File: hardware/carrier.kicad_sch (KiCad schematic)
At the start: 58 parts, among them J2 Heltec_J2, J3 Heltec_J3, U1 MT3608, U2 TCA9534PWR, U3 MAX98357A

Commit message: hardware: regenerate for 4-pin XH, add XB8089D cell protection, power model
Regenerated with KiCad 9 after the cloud parts review (make all: ERC 0, DRC 0,
0 unrouted). Six 4-pin XH connectors do not fit the top edge, so J_BTN_R1 moves
to the bottom edge under J2; the schematic connectors shift because Conn_01x04
anchors on pin 2. Two-wire connectors label only pins 1-2 on silk.

The Heltec V4.2 schematic shows no under-voltage cutoff (CN3165 charger, Q4 is
reverse-polarity only), so U4 XB8089D (C79928) goes in the cell negative lead
with R_PROT1 1k / C_PROT1 100nF. Symbol lives in the project lib local.kicad_sym.

power_budget.py estimates runtime per scenario from the Heltec datasheet and
marked estimates (~25 h Deluxe game with backlight, ~40 h without).

Co-Authored-By: Claude Opus 5.5 <noreply@anthropic.com>
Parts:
- added C_PROT1: 100nF, Capacitor_SMD:C_0805_2012Metric_Pad1.18x1.45mm_HandSolder, symbol Device:C
- added R_PROT1: 1k, Resistor_SMD:R_0805_2012Metric_Pad1.20x1.40mm_HandSolder, symbol Device:R
- added U4: XB8089D, Package_SO:SOIC-8-1EP_3.9x4.9mm_P1.27mm_EP2.41x3.3mm, symbol local:XB8089D
- J_BAT1, J_BUZ1, J_HBAT1, J_KEY1, J_SPK1: footprint Connector_JST:JST_XH_B2B-XH-A_1x02_P2.50mm_Vertical -> Connector_JST:JST_XH_B4B-XH-A_1x04_P2.50mm_Vertical; symbol Connector_Generic:Conn_01x02 -> Connector_Generic:Conn_01x04
- Q_BZ1, Q_LB1, Q_LR1: value AO3400A -> BSS138; symbol Transistor_FET:AO3400A -> Transistor_FET:BSS138
- R_GBZ1, R_GLB1, R_GLR1: value 100R -> 1k
- R_PDBZ1, R_PDLB1, R_PDLR1: value 100k -> 10k
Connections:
- net GND: now also U4.1 (VM), U4.2 (VM), U4.3 (VM), U4.4 (VM); no longer J_BAT1.2 (Pin_2)
- net VBAT_RAW: now also R_PROT1.1
- new net BAT_N: C_PROT1.2, J_BAT1.2 (Pin_2), U4.5 (GND), U4.7 (GND), U4.8 (GND), U4.9 (EPAD)
- new net PROT_VDD: C_PROT1.1, R_PROT1.2, U4.6 (VDD)
- no-connect marks 33 -> 43
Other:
- moved on the sheet: C_AMP1, C_AMP2, F1

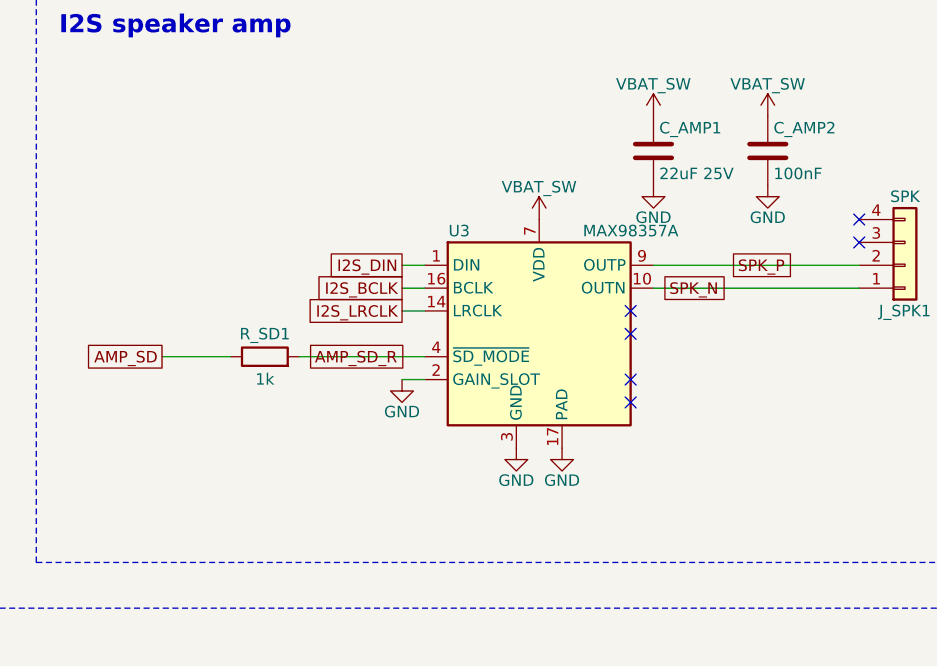
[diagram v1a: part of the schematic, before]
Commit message: hardware: replace MAX98357A with NS4168 I2S amp
U3 becomes an NS4168 (C910588, eSOP-8, ~$0.95 cheaper per board, same
Extended setup fee). CTRL high selects the right I2S slot, so firmware must
send audio in the right slot (or both) and hold CTRL low between clips
(13 mA when on). R_SD1 stays in series (CTRL abs max is VDD); new R_SDPD1 10k
on AMP_SD keeps the amp off while the expander floats at reset. C_AMP1 is now
100 uF per the datasheet. Both reuse existing BOM lines.

make all: ERC 0, DRC 0, 0 unrouted. Deluxe 20 BOM lines, Budget 19.

Co-Authored-By: Claude Opus 5.5 <noreply@anthropic.com>
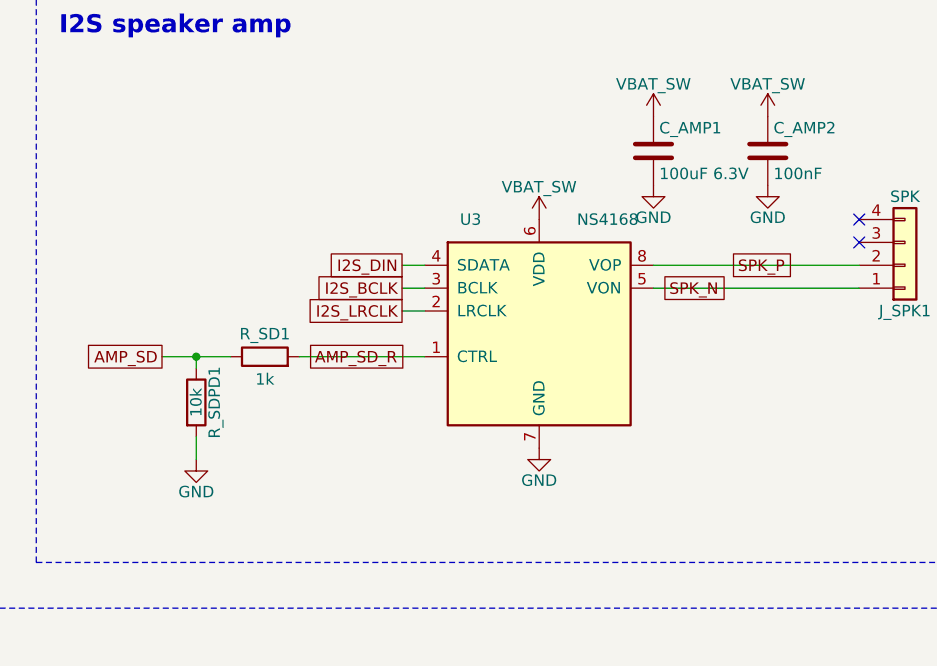
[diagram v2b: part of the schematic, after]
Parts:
- added R_SDPD1: 10k, Resistor_SMD:R_0805_2012Metric_Pad1.20x1.40mm_HandSolder, symbol Device:R
- C_AMP1: value 22uF 25V -> 100uF 6.3V
- U3: value MAX98357A -> NS4168; footprint Package_DFN_QFN:TQFN-16-1EP_3x3mm_P0.5mm_EP1.23x1.23mm_ThermalVias -> Package_SO:HSOP-8-1EP_3.9x4.9mm_P1.27mm_EP2.3x2.3mm_ThermalVias; symbol Audio:MAX98357A -> local:NS4168
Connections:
- net AMP_SD: now also R_SDPD1.1
- net AMP_SD_R: now also U3.1 (CTRL); no longer U3.4 (~{SD_MODE})
- net GND: now also U3.7 (GND), U3.9 (EP), R_SDPD1.2; no longer U3.11 (GND), U3.15 (GND), U3.17 (PAD), U3.2 (GAIN_SLOT), U3.3 (GND)
- net I2S_BCLK: now also U3.3 (BCLK); no longer U3.16 (BCLK)
- net I2S_DIN: now also U3.4 (SDATA); no longer U3.1 (DIN)
- net I2S_LRCLK: now also U3.2 (LRCLK); no longer U3.14 (LRCLK)
- net SPK_N: now also U3.5 (VON); no longer U3.10 (OUTN)
- net SPK_P: now also U3.8 (VOP); no longer U3.9 (OUTP)
- net VBAT_SW: now also U3.6 (VDD); no longer U3.7 (VDD), U3.8 (VDD)
- no-connect marks 43 -> 39

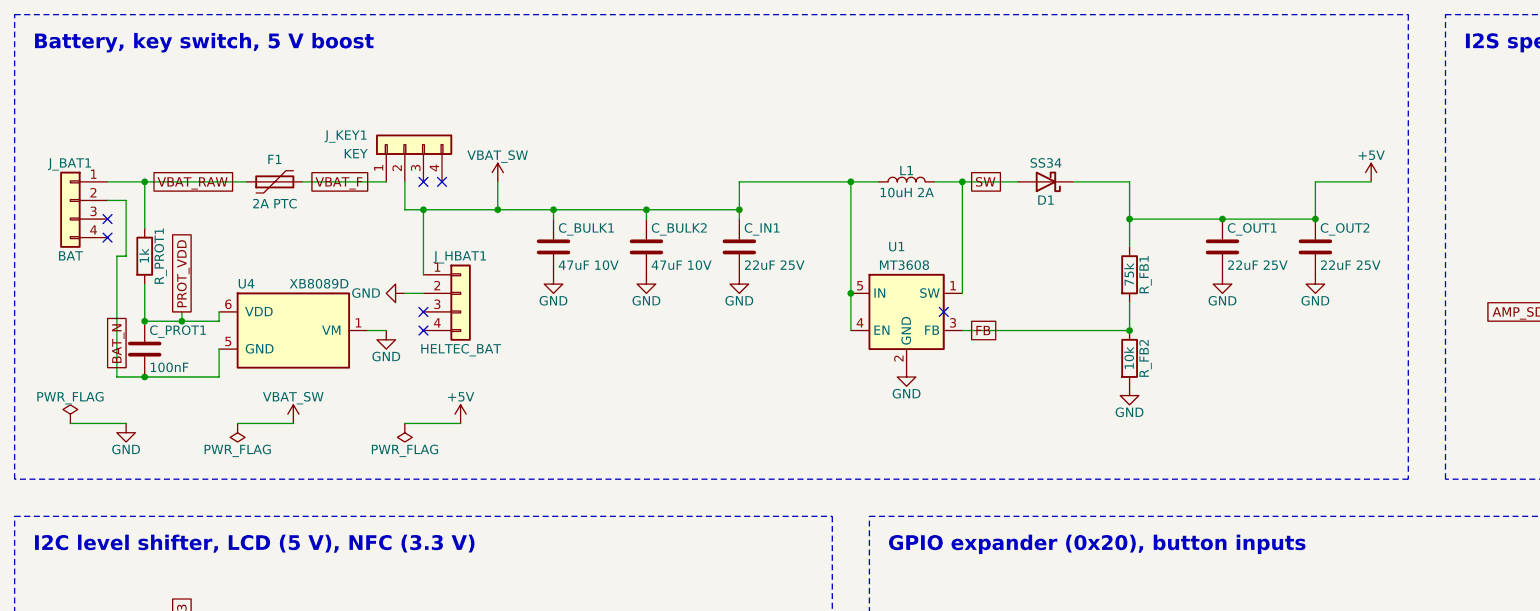
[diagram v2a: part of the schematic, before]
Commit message: hardware: carrier takes power from the pack board (P5)
The cell protector, key switch, 5 V boost and their parts move to the pack
board; the carrier gets a 6-pin J_PWR1 (GND GND VBAT_SW +5V SDA_3V3 SCL_3V3).
The first block is now "Power in (from pack board)" and does not wire its
rails, so every rail pin gets its own power port.

make BOARD=carrier all is green (ERC, DRC parity, gerbers, jlc).

Co-Authored-By: Claude Opus 5.5 <noreply@anthropic.com>
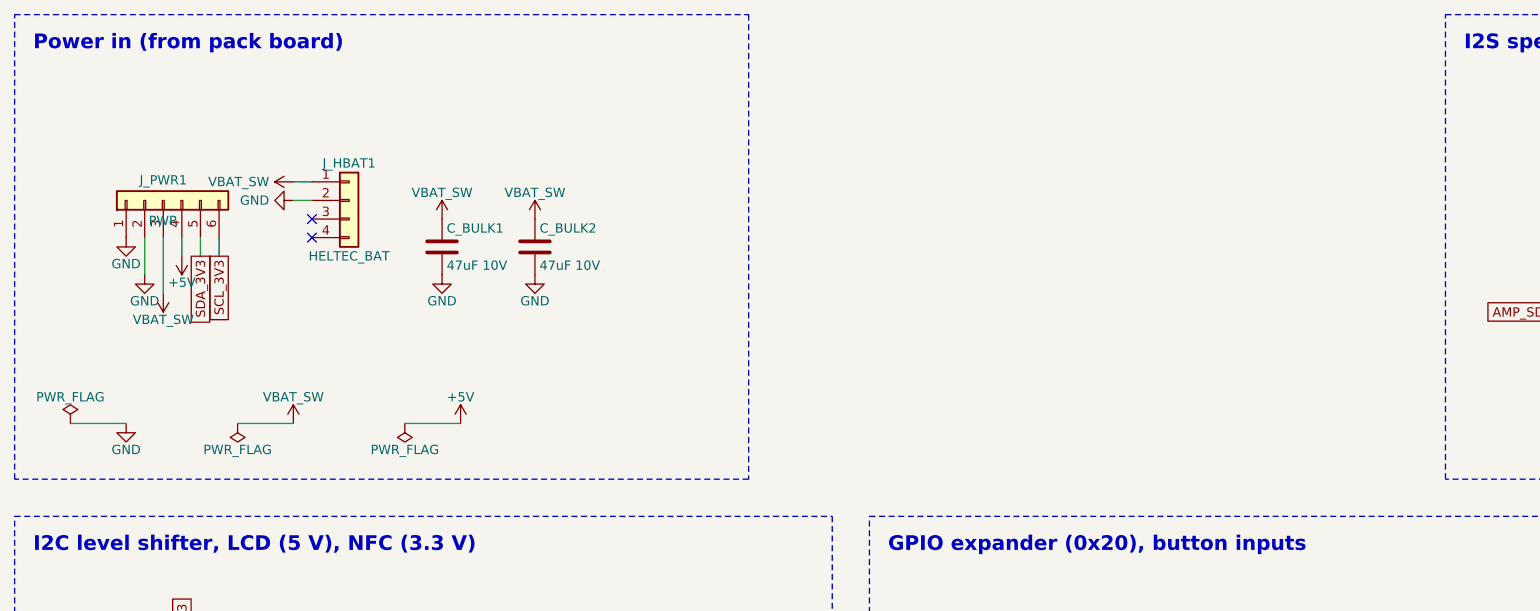
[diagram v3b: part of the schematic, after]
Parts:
- removed C_IN1, C_OUT1, C_OUT2: 22uF 25V, Capacitor_SMD:C_1206_3216Metric_Pad1.33x1.80mm_HandSolder, symbol Device:C
- removed C_PROT1: 100nF, Capacitor_SMD:C_0805_2012Metric_Pad1.18x1.45mm_HandSolder, symbol Device:C
- removed D1: SS34, Diode_SMD:D_SMA, symbol Diode:SS34
- removed F1: 2A PTC, Fuse:Fuse_1206_3216Metric_Pad1.42x1.75mm_HandSolder, symbol Device:Polyfuse
- removed J_BAT1: BAT, Connector_JST:JST_XH_B4B-XH-A_1x04_P2.50mm_Vertical, symbol Connector_Generic:Conn_01x04
- removed J_KEY1: KEY, Connector_JST:JST_XH_B4B-XH-A_1x04_P2.50mm_Vertical, symbol Connector_Generic:Conn_01x04
- removed L1: 10uH 2A, Inductor_SMD:L_Bourns_SRN6045TA, symbol Device:L
- removed R_FB1: 75k, Resistor_SMD:R_0805_2012Metric_Pad1.20x1.40mm_HandSolder, symbol Device:R
- removed R_FB2: 10k, Resistor_SMD:R_0805_2012Metric_Pad1.20x1.40mm_HandSolder, symbol Device:R
- removed R_PROT1: 1k, Resistor_SMD:R_0805_2012Metric_Pad1.20x1.40mm_HandSolder, symbol Device:R
- removed U1: MT3608, Package_TO_SOT_SMD:SOT-23-6, symbol Regulator_Switching:MT3608
- removed U4: XB8089D, Package_SO:SOIC-8-1EP_3.9x4.9mm_P1.27mm_EP2.41x3.3mm, symbol local:XB8089D
- added J_PWR1: PWR, Connector_JST:JST_XH_B6B-XH-A_1x06_P2.50mm_Vertical, symbol Connector_Generic:Conn_01x06
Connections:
- net +5V: now also J_PWR1.4 (Pin_4)
- net GND: now also J_PWR1.1 (Pin_1), J_PWR1.2 (Pin_2)
- net SCL_3V3: now also J_PWR1.6 (Pin_6)
- net SDA_3V3: now also J_PWR1.5 (Pin_5)
- net VBAT_SW: now also J_PWR1.3 (Pin_3)
- no-connect marks 39 -> 34
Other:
- note added: "Power in (from pack board)"
- note removed: "Battery, key switch, 5 V boost"
- moved on the sheet: C_BULK1, C_BULK2, J_HBAT1
